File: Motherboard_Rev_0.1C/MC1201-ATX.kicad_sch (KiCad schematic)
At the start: 251 parts, among them J1 PLD-16, J2 PLD-16, J3 PLD-16, J4 ATX-20, J5 Conn_01x01_Pin, J6 Conn_01x01_Pin, J7 Conn_01x09_Pin, P1 Conn_01x01_Pin, P10 Conn_01x01_Pin, P11 Conn_01x01_Pin, P12 Conn_01x01_Pin, P13 Conn_01x01_Pin, P14 Conn_01x01_Pin, P15 Conn_01x01_Pin, P16 Conn_01x01_Pin, P17 Conn_01x01_Pin, P18 Conn_01x01_Pin, P2 Conn_01x01_Pin, P3 Conn_01x01_Pin, P4 Conn_01x01_Pin, P5 Conn_01x01_Pin, P6 Conn_01x01_Pin, P7 Conn_01x01_Pin, P8 Conn_01x01_Pin, P9 Conn_01x01_Pin, Q1 BC547, X2 AFPC, X3 QBUS_DWK_64Pin_MBT

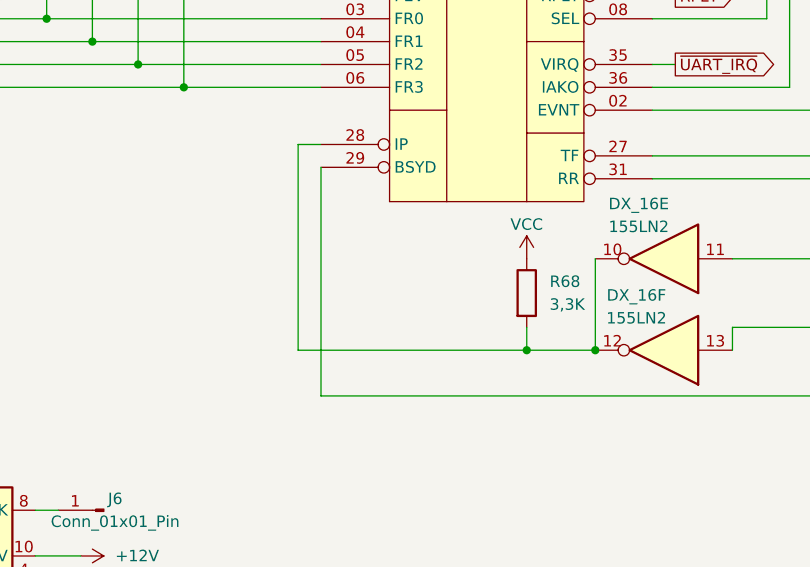
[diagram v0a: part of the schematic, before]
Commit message: Found and documented erratum 0011
Serial port receive now works. The machine is fully commissioned.
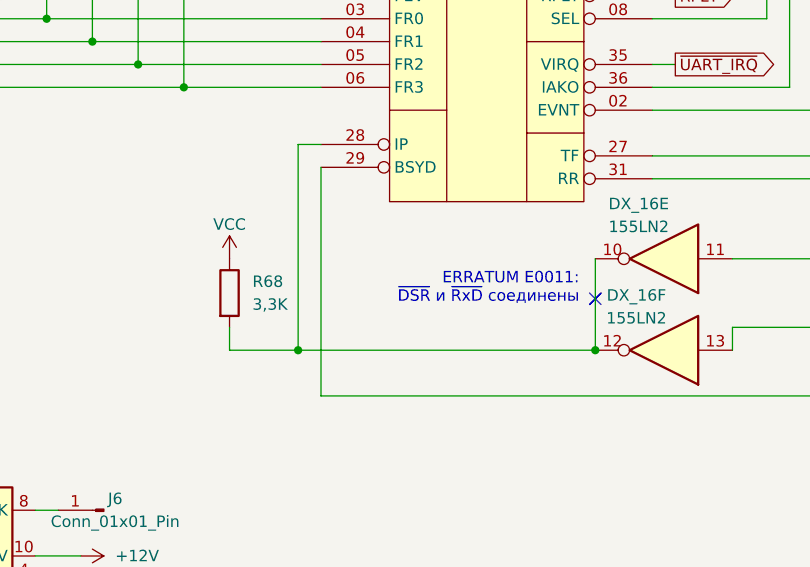
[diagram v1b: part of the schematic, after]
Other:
- note added: "ERRATUM E0011: ~{DSR} и ~{RxD} соединены"
- moved on the sheet: R68
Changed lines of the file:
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@@
 		)
 	)
+	(text "ERRATUM E0011:\n~{DSR} и ~{RxD} соединены"
+		(exclude_from_sim no)
+		(at 407.162 336.042 0)
+		(effects
+			(font
+				(size 1.27 1.27)
+				(color 255 0 0 1)
+			)
+			(justify right)
+		)
+	)
 	(text "Питание и фильтры"
 		(exclude_from_sim no)
@@
 	)
 	(junction
+		(at 375.92 342.9)
+		(diameter 0)
+		(color 0 0 0 0)
+	)
+	(junction
 		(at 486.41 36.83)
 		(diameter 0)
@@
 	)
 	(junction
-		(at 401.32 342.9)
-		(diameter 0)
-		(color 0 0 0 0)
-	)
-	(junction
 		(at 482.6 351.79)
 		(diameter 0)
@@
 	(wire
 		(pts
-			(xy 401.32 342.9) (xy 401.32 340.36)
+			(xy 368.3 342.9) (xy 368.3 340.36)
 		)
 		(stroke
@@
 		)
 	)
+	(polyline
+		(pts
+			(xy 409.575 336.55) (xy 408.305 337.82)
+		)
+		(stroke
+			(width 0)
+			(type solid)
+			(color 255 0 0 1)
+		)
+	)
 	(wire
 		(pts
@@
 	(wire
 		(pts
-			(xy 401.32 342.9) (xy 408.94 342.9)
-		)
-		(stroke
-			(width 0)
-			(type default)
-		)
-	)
-	(wire
-		(pts
 			(xy 149.86 336.55) (xy 165.1 336.55)
 		)
@@
 	(wire
 		(pts
-			(xy 401.32 342.9) (xy 375.92 342.9)
+			(xy 375.92 342.9) (xy 408.94 342.9)
 		)
 		(stroke
@@
 	(wire
 		(pts
+			(xy 368.3 342.9) (xy 375.92 342.9)
+		)
+		(stroke
+			(width 0)
+			(type default)
+		)
+	)
+	(wire
+		(pts
 			(xy 351.79 246.38) (xy 351.79 255.27)
 		)
@@
 		)
 	)
+	(polyline
+		(pts
+			(xy 408.305 336.55) (xy 409.575 337.82)
+		)
+		(stroke
+			(width 0)
+			(type solid)
+			(color 255 0 0 1)
+		)
+	)
 	(wire
 		(pts
@@
 		)
 	)
+	(polyline
+		(pts
+			(xy 408.305 337.82) (xy 409.575 336.55)
+		)
+		(stroke
+			(width 0)
+			(type solid)
+			(color 255 0 0 1)
+		)
+	)
 	(wire
 		(pts
@@
 	(symbol
 		(lib_id "Device:R")
-		(at 401.32 336.55 0)
+		(at 368.3 336.55 0)
 		(unit 1)
 		(body_style 1)
@@
 		(fields_autoplaced yes)
 		(property "Reference" "R68"
-			(at 403.86 335.2799 0)
+			(at 370.84 335.2799 0)
 			(show_name no)
 			(do_not_autoplace no)
@@
 		)
 		(property "Value" "3,3K"
-			(at 403.86 337.8199 0)
+			(at 370.84 337.8199 0)
 			(show_name no)
 			(do_not_autoplace no)
@@
 		)
 		(property "Footprint" "Resistor_THT:R_Axial_DIN0204_L3.6mm_D1.6mm_P7.62mm_Horizontal"
-			(at 399.542 336.55 90)
+			(at 366.522 336.55 90)
 			(hide yes)
 			(show_name no)
@@
 		)
 		(property "Datasheet" ""
-			(at 401.32 336.55 0)
+			(at 368.3 336.55 0)
 			(hide yes)
 			(show_name no)
@@
 		)
 		(property "Description" "Resistor"
-			(at 401.32 336.55 0)
+			(at 368.3 336.55 0)
 			(hide yes)
 			(show_name no)
@@
 	(symbol
 		(lib_id "power:VCC")
-		(at 401.32 332.74 0)
+		(at 368.3 332.74 0)
 		(unit 1)
 		(body_style 1)
@@
 		(dnp no)
 		(property "Reference" "#PWR075"
-			(at 401.32 336.55 0)
+			(at 368.3 336.55 0)
 			(hide yes)
 			(show_name no)
@@
 		)
 		(property "Value" "VCC"
-			(at 401.32 328.93 0)
+			(at 368.3 328.93 0)
 			(show_name no)
 			(do_not_autoplace no)
@@
 		)
 		(property "Footprint" ""
-			(at 401.32 332.74 0)
+			(at 368.3 332.74 0)
 			(hide yes)
 			(show_name no)
@@
 		)
 		(property "Datasheet" ""
-			(at 401.32 332.74 0)
+			(at 368.3 332.74 0)
 			(hide yes)
 			(show_name no)
@@
 		)
 		(property "Description" "Power symbol creates a global label with name \"VCC\""
-			(at 401.32 332.74 0)
+			(at 368.3 332.74 0)
 			(hide yes)
 			(show_name no)

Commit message: Completed schematic validation
Some clarifications, some more DNPs. Proper value of RX1 = 10K.
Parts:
- DXD1: value 1N4148 -> 100K; symbol Diode:1N4148 -> Device:R
- EX2_8, RX2: now not fitted
- RX1: value 47K -> 10K
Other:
- note added: "В оригинальной схеме в поз. DXD1 стоит диод, но в этом нет смысла."
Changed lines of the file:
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@@
 		)
 	)
+	(text "В оригинальной схеме в\nпоз. DXD1 стоит диод, но\nв этом нет смысла."
+		(exclude_from_sim no)
+		(at 347.218 24.384 0)
+		(effects
+			(font
+				(size 1.27 1.27)
+			)
+			(justify right)
+		)
+	)
 	(text "Элементы, помеченные\nкак \"не устанавливать\",\nиспользуются в оригинальной\nсхеме для связи с силовым\nинтерфейсом МПИ, который\nв данной схеме отсутствует\n(если не указано иное)"
 		(exclude_from_sim no)
@@
 		(on_board yes)
 		(in_pos_files yes)
-		(dnp no)
+		(dnp yes)
 		(property "Reference" "RX2"
 			(at 343.916 59.69 0)
@@
 			)
 		)
-		(property "Value" "47K"
+		(property "Value" "10K"
 			(at 187.96 50.7999 0)
 			(show_name no)
@@
 		(on_board yes)
 		(in_pos_files yes)
-		(dnp no)
+		(dnp yes)
 		(property "Reference" "EX2_8"
 			(at 328.422 148.336 90)
@@
 	)
 	(symbol
-		(lib_id "Diode:1N4148")
-		(at 349.25 27.94 90)
+		(lib_id "Device:R")
+		(at 349.25 27.94 180)
 		(unit 1)
 		(body_style 1)
@@
 		(fields_autoplaced yes)
 		(property "Reference" "DXD1"
-			(at 351.79 26.6699 90)
+			(at 351.79 26.6699 0)
 			(show_name no)
 			(do_not_autoplace no)
@@
 			)
 		)
-		(property "Value" "1N4148"
-			(at 351.79 29.2099 90)
+		(property "Value" "100K"
+			(at 351.79 29.2099 0)
 			(show_name no)
 			(do_not_autoplace no)
@@
 		)
 		(property "Footprint" "Diode_THT:D_DO-35_SOD27_P7.62mm_Horizontal"
-			(at 349.25 27.94 0)
+			(at 351.028 27.94 90)
 			(hide yes)
 			(show_name no)
@@
 			)
 		)
-		(property "Description" "100V 0.15A standard switching diode, DO-35"
+		(property "Description" "Resistor"
 			(at 349.25 27.94 0)
 			(hide yes)

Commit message: Mezzanine board schematic
A board, containing the missing parts of the schematic plus full-featured Q-Bus.
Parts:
- C70, DD44, E4_7, E5_5, E7_1, E9_9, R8, S13: now fitted
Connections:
- net ~{EXT_IRQ2}: now reaches DD44.2 (D), E5_5.2
- net ~{ROM_DIN}: now reaches DD9.10, DS1.01 (DIN), E8_5.2
- net ~{EXT_SYNC}: now reaches DD18.1 (~{R}), DD18.2 (D), E6_4.2
- net ~{EXT_WTBT}: now reaches DD20.8, E7_1.2
- net ~{EXT_DMR}: now reaches DD44.12 (D), E4_7.2, S13.1 (Pin_1)
- net ~{EXT_DMG}: now reaches DD8.9 (Q), E9_9.2
- net ~{UART_IRQ} renamed ~{EXT_VIRQ}
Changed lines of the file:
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@@
 	(text "ERRATUM E0006\nЛишний резистор"
 		(exclude_from_sim no)
-		(at 35.306 118.618 0)
+		(at 34.544 106.934 0)
 		(effects
 			(font
@@
 	)
 	(junction
-		(at 50.8 215.9)
-		(diameter 0)
-		(color 0 0 0 0)
-	)
-	(junction
 		(at 63.5 39.37)
 		(diameter 0)
@@
 	)
 	(junction
+		(at 50.8 198.12)
+		(diameter 0)
+		(color 0 0 0 0)
+	)
+	(junction
 		(at 541.02 78.74)
 		(diameter 0)
@@
 	)
 	(junction
+		(at 181.61 124.46)
+		(diameter 0)
+		(color 0 0 0 0)
+	)
+	(junction
 		(at 104.14 63.5)
 		(diameter 0)
@@
 	)
 	(junction
+		(at 88.9 154.94)
+		(diameter 0)
+		(color 0 0 0 0)
+	)
+	(junction
 		(at 486.41 77.47)
 		(diameter 0)
@@
 	)
 	(junction
+		(at 50.8 215.9)
+		(diameter 0)
+		(color 0 0 0 0)
+	)
+	(junction
 		(at 382.27 158.75)
 		(diameter 0)
@@
 	(wire
 		(pts
-			(xy 45.72 215.9) (xy 50.8 215.9)
+			(xy 39.37 215.9) (xy 50.8 215.9)
 		)
 		(stroke
@@
 	(wire
 		(pts
+			(xy 46.99 198.12) (xy 50.8 198.12)
+		)
+		(stroke
+			(width 0)
+			(type default)
+		)
+	)
+	(wire
+		(pts
 			(xy 523.24 153.67) (xy 528.32 153.67)
 		)
@@
 	(wire
 		(pts
+			(xy 88.9 154.94) (xy 99.06 154.94)
+		)
+		(stroke
+			(width 0)
+			(type default)
+		)
+	)
+	(wire
+		(pts
 			(xy 91.44 73.66) (xy 90.17 73.66)
 		)
@@
 	(wire
 		(pts
+			(xy 34.29 116.84) (xy 50.8 116.84)
+		)
+		(stroke
+			(width 0)
+			(type default)
+		)
+	)
+	(wire
+		(pts
 			(xy 501.65 294.64) (xy 502.92 294.64)
 		)
@@
 	(wire
 		(pts
+			(xy 181.61 124.46) (xy 184.15 124.46)
+		)
+		(stroke
+			(width 0)
+			(type default)
+		)
+	)
+	(wire
+		(pts
 			(xy 523.24 161.29) (xy 528.32 161.29)
 		)
@@
 		)
 	)
+	(label "~{EXT_DMR}"
+		(at 39.37 215.9 0)
+		(effects
+			(font
+				(size 1.27 1.27)
+			)
+			(justify left bottom)
+		)
+	)
 	(label "~{A10}"
 		(at 254 116.84 0)
@@
 		)
 	)
+	(label "~{ROM_DIN}"
+		(at 205.105 243.84 0)
+		(effects
+			(font
+				(size 1.27 1.27)
+			)
+			(justify left bottom)
+		)
+	)
 	(label "~{B15}"
 		(at 502.92 113.03 180)
@@
 		)
 	)
+	(global_label "~{EXT_IRQ2}"
+		(shape input)
+		(at 46.99 198.12 180)
+		(fields_autoplaced yes)
+		(effects
+			(font
+				(size 1.27 1.27)
+			)
+			(justify right)
+		)
+		(property "Intersheetrefs" "${INTERSHEET_REFS}"
+			(at 35.2963 198.12 0)
+			(hide yes)
+			(show_name no)
+			(do_not_autoplace no)
+			(effects
+				(font
+					(size 1.27 1.27)
+				)
+				(justify right)
+			)
+		)
+	)
 	(global_label "~{DOUT}"
 		(shape input)
@@
 		)
 	)
+	(global_label "~{EXT_SYNC}"
+		(shape input)
+		(at 34.29 116.84 180)
+		(fields_autoplaced yes)
+		(effects
+			(font
+				(size 1.27 1.27)
+			)
+			(justify right)
+		)
+		(property "Intersheetrefs" "${INTERSHEET_REFS}"
+			(at 22.1125 116.84 0)
+			(hide yes)
+			(show_name no)
+			(do_not_autoplace no)
+			(effects
+				(font
+					(size 1.27 1.27)
+				)
+				(justify right)
+			)
+		)
+	)
 	(global_label "~{DMR}"
 		(shape passive)
@@
 		)
 	)
+	(global_label "~{EXT_WTBT}"
+		(shape output)
+		(at 184.15 124.46 0)
+		(fields_autoplaced yes)
+		(effects
+			(font
+				(size 1.27 1.27)
+			)
+			(justify left)
+		)
+		(property "Intersheetrefs" "${INTERSHEET_REFS}"
+			(at 196.0855 124.46 0)
+			(hide yes)
+			(show_name no)
+			(do_not_autoplace no)
+			(effects
+				(font
+					(size 1.27 1.27)
+				)
+				(justify left)
+			)
+		)
+	)
 	(global_label "~{RPLY}"
 		(shape output)
@@
 		)
 	)
+	(global_label "~{EXT_DMG}"
+		(shape output)
+		(at 99.06 154.94 0)
+		(fields_autoplaced yes)
+		(effects
+			(font
+				(size 1.27 1.27)
+			)
+			(justify left)
+		)
+		(property "Intersheetrefs" "${INTERSHEET_REFS}"
+			(at 110.3303 154.94 0)
+			(hide yes)
+			(show_name no)
+			(do_not_autoplace no)
+			(effects
+				(font
+					(size 1.27 1.27)
+				)
+				(justify left)
+			)
+		)
+	)
 	(global_label "~{DMR}"
 		(shape input)
@@
 		)
 	)
-	(global_label "~{UART_IRQ}"
+	(global_label "~{EXT_VIRQ}"
 		(shape output)
 		(at 417.83 311.15 0)
@@
 		)
 		(property "Intersheetrefs" "${INTERSHEET_REFS}"
-			(at 429.6448 311.15 0)
+			(at 429.4028 311.15 0)
 			(hide yes)
 			(show_name no)
@@
 		)
 	)
-	(global_label "~{UART_IRQ}"
+	(global_label "~{EXT_VIRQ}"
 		(shape input)
 		(at 46.99 180.34 180)
@@
 		)
 		(property "Intersheetrefs" "${INTERSHEET_REFS}"
-			(at 35.1752 180.34 0)
+			(at 35.4172 180.34 0)
 			(hide yes)
 			(show_name no)
@@
 		(on_board yes)
 		(in_pos_files yes)
-		(dnp yes)
+		(dnp no)
 		(property "Reference" "E5_5"
 			(at 52.324 193.294 0)
@@
 	(symbol
 		(lib_id "Connector:Conn_01x01_Pin")
-		(at 40.64 215.9 0)
+		(at 34.29 215.9 0)
 		(unit 1)
 		(body_style 1)
@@
 		(on_board yes)
 		(in_pos_files yes)
-		(dnp yes)
-		(fields_autoplaced yes)
+		(dnp no)
 		(property "Reference" "S13"
-			(at 41.275 210.82 0)
+			(at 34.925 210.82 0)
 			(show_name no)
 			(do_not_autoplace no)
@@
 		)
 		(property "Value" "Conn_01x01_Pin"
-			(at 41.275 213.36 0)
+			(at 29.972 213.36 0)
 			(show_name no)
 			(do_not_autoplace no)
@@
 		)
 		(property "Footprint" "Connector_PinHeader_2.54mm:PinHeader_1x01_P2.54mm_Vertical"
-			(at 40.64 215.9 0)
+			(at 34.29 215.9 0)
 			(hide yes)
 			(show_name no)
@@
 		)
 		(property "Datasheet" ""
-			(at 40.64 215.9 0)
+			(at 34.29 215.9 0)
 			(hide yes)
 			(show_name no)
@@
 		)
 		(property "Description" "Generic connector, single row, 01x01, script generated"
-			(at 40.64 215.9 0)
+			(at 34.29 215.9 0)
 			(hide yes)
 			(show_name no)
@@
 		(on_board yes)
 		(in_pos_files yes)
-		(dnp yes)
+		(dnp no)
 		(property "Reference" "E4_7"
 			(at 52.324 210.82 0)
@@
 		(on_board yes)
 		(in_pos_files yes)
-		(dnp yes)
+		(dnp no)
 		(fields_autoplaced yes)
 		(property "Reference" "E7_1"
@@
 		(on_board yes)
 		(in_pos_files yes)
-		(dnp yes)
+		(dnp no)
 		(fields_autoplaced yes)
 		(property "Reference" "E9_9"
@@
 		(on_board yes)
 		(in_pos_files yes)
-		(dnp yes)
+		(dnp no)
 		(fields_autoplaced yes)
 		(property "Reference" "DD44"
@@
 		(on_board yes)
 		(in_pos_files yes)
-		(dnp yes)
+		(dnp no)
 		(fields_autoplaced yes)
 		(property "Reference" "DD44"
@@
 		(on_board yes)
 		(in_pos_files yes)
-		(dnp yes)
+		(dnp no)
 		(property "Reference" "R8"
 			(at 154.94 119.888 90)
@@
 		(on_board yes)
 		(in_pos_files yes)
-		(dnp yes)
+		(dnp no)
 		(property "Reference" "C70"
 			(at 164.338 127 0)
